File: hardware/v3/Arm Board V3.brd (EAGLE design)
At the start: 165.1 x 76.2 mm, 75 parts, among them CN1 1X4-BIG, IC1 L6208D, IC2 L6208D, IC3 L6208D, IC4 7812TV, IC5 7812TV, IC6 7812TV, IC7 7812DT, IC9 7812DT, Q3 Q_LTC490, U1 MAX3468CPA, U2 XBEE-1B3

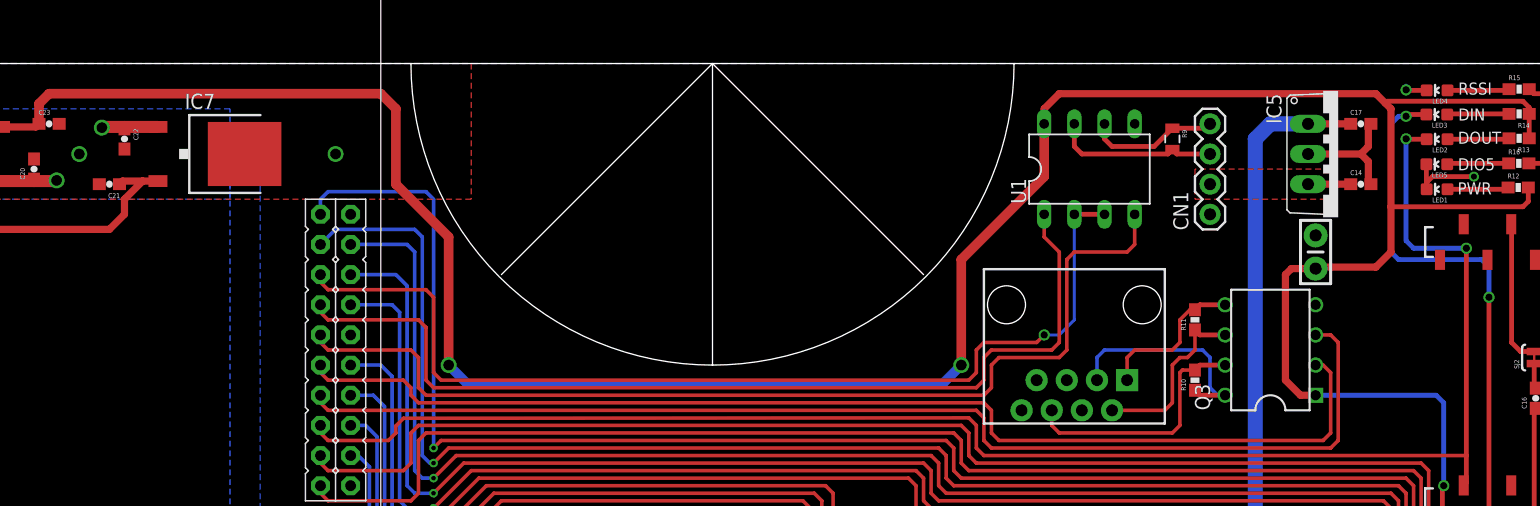
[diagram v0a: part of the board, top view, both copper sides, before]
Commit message: Changed name on l6208 to l6206
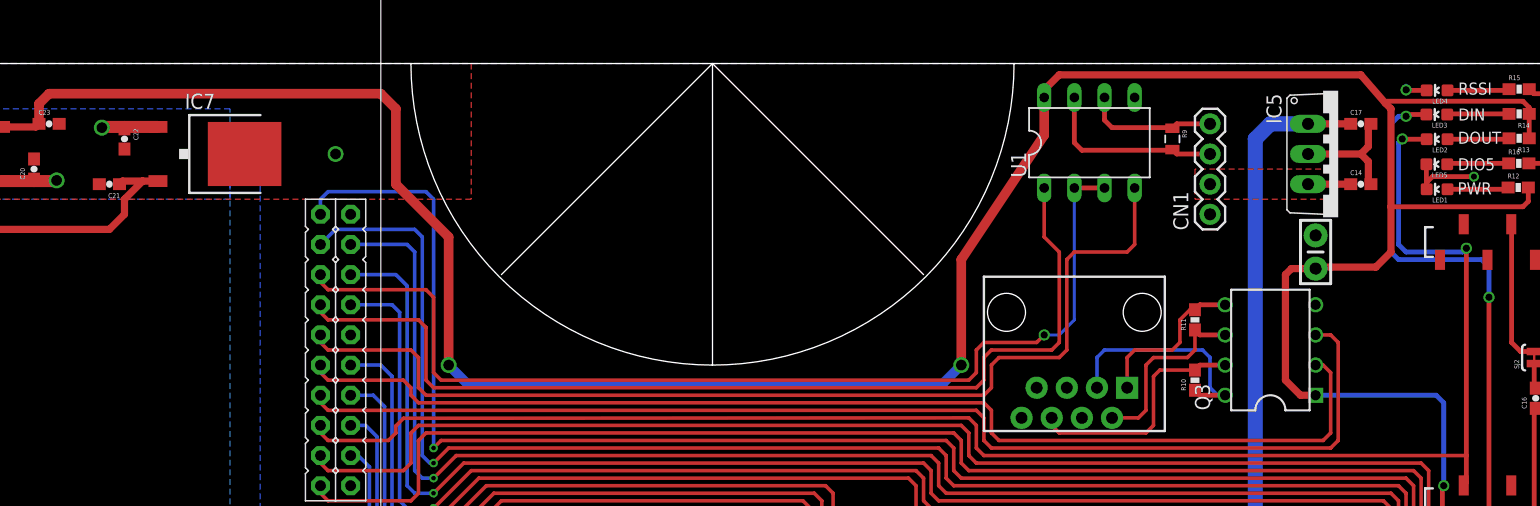
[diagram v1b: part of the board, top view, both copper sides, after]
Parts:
- IC1, IC2, IC3: value L6208D -> L6206D
- moved U1 2.22 mm to (114.3, 69.5)
- moved U$3 0.64 mm to (113.0, 55.2)
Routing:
- net TXD2: track 85.9 -> 88.1 mm
- net RXD2: track 82.1 -> 84.3 mm
- net EN485: track 85.9 -> 88.1 mm
- net DD+: track 13.9 -> 15.7 mm
- net +3V3: track 266.9 -> 268.5 mm
- net RXD3: track 136.7 -> 138.2 mm
- net N$2: track 21.1 -> 20.3 mm
- net N$1: track 15.7 -> 16.3 mm
- net N$5: track 13.1 -> 13.8 mm
- net N$3: track 18.7 -> 19.4 mm
- net GND: vias 9 -> 8

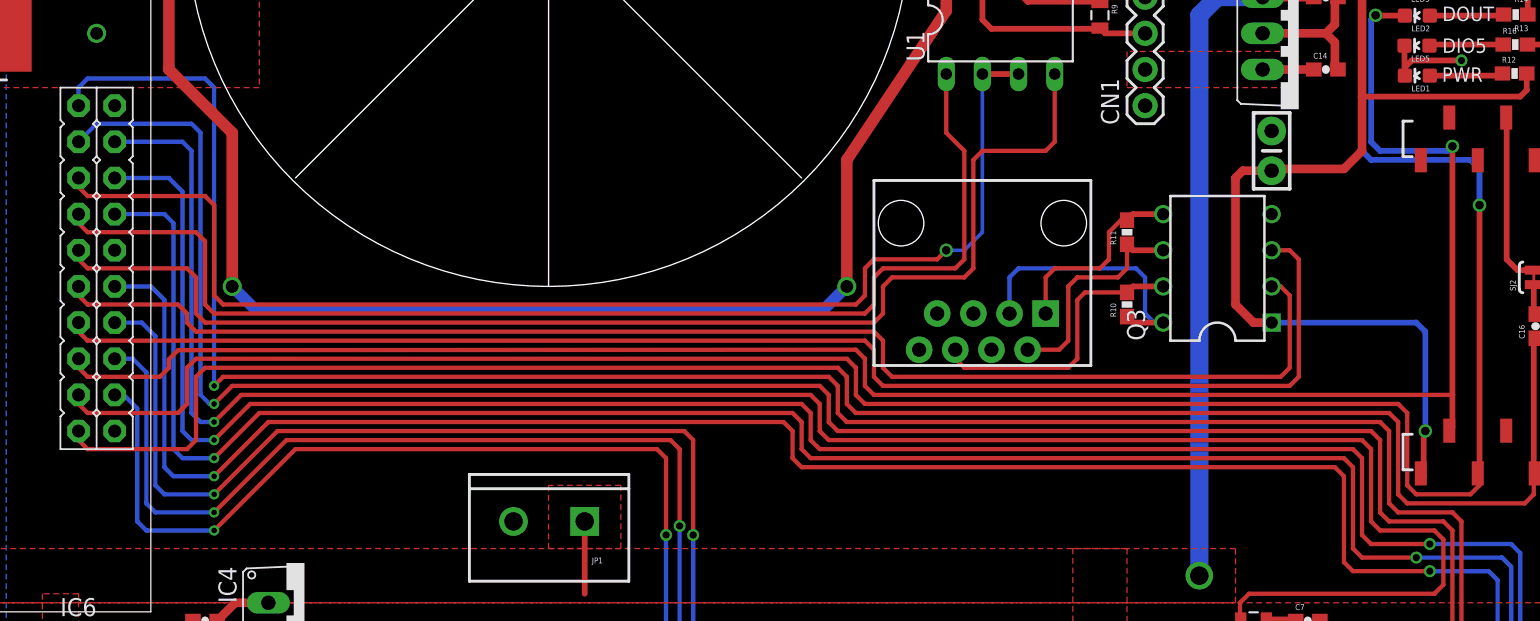
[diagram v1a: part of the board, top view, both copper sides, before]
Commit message: Moved Data Lines closer together
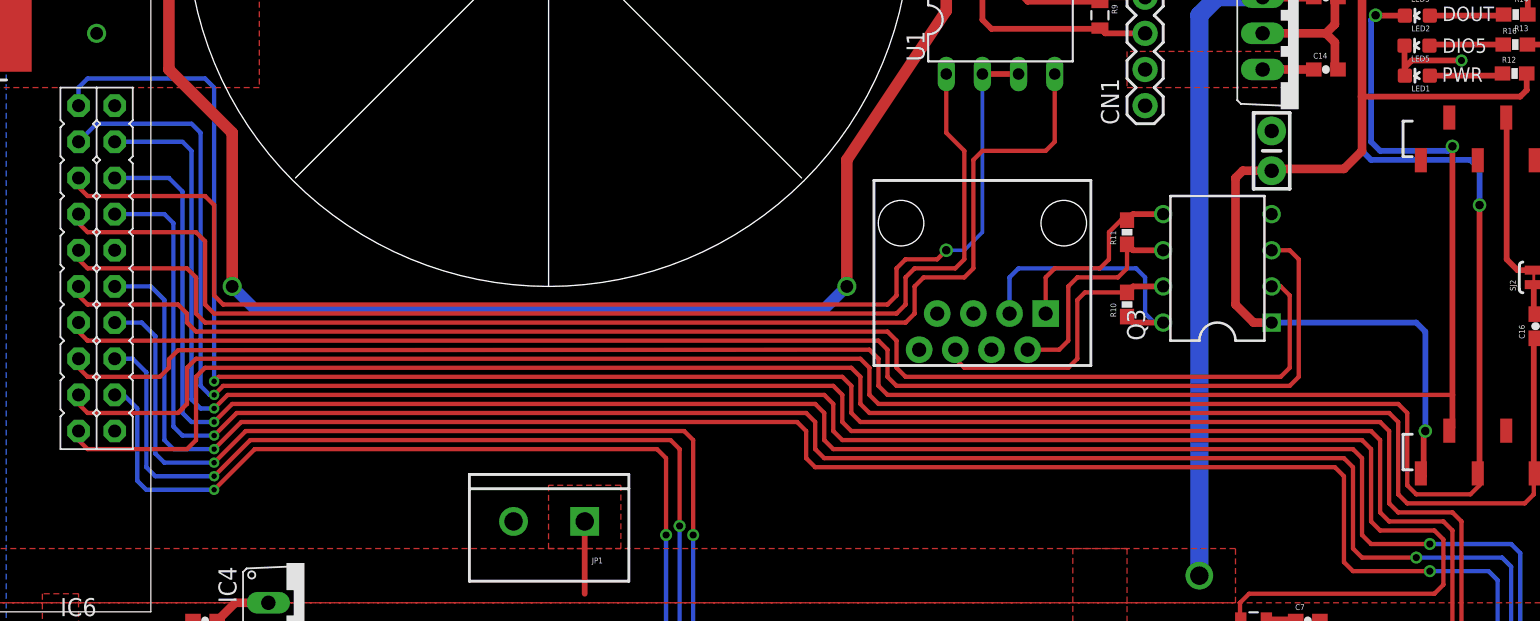
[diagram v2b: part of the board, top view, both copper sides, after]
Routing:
- net IN1_A_3: track 82.5 -> 78.4 mm
- net IN2_A_3: track 85.6 -> 82.0 mm
- net EN_A_3: track 86.3 -> 83.2 mm
- net EN_A_2: track 142.0 -> 139.3 mm
- net IN2_A_2: track 153.1 -> 150.8 mm
- net IN1_A_2: track 156.9 -> 155.1 mm
- net EN_B_2: track 140.7 -> 139.3 mm
- net IN2_B_2: track 135.5 -> 134.6 mm

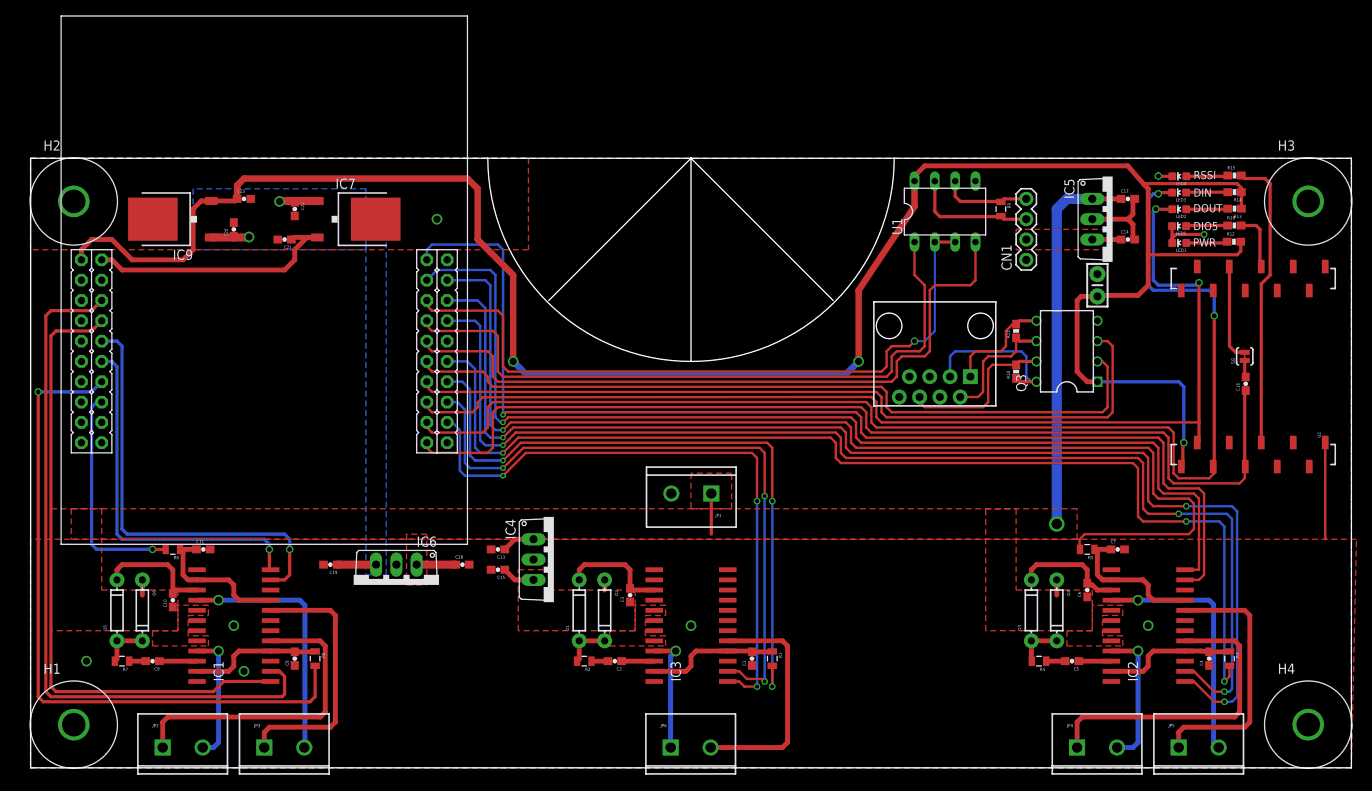
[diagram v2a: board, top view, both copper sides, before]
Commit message: Finished assigning values and fixing errors
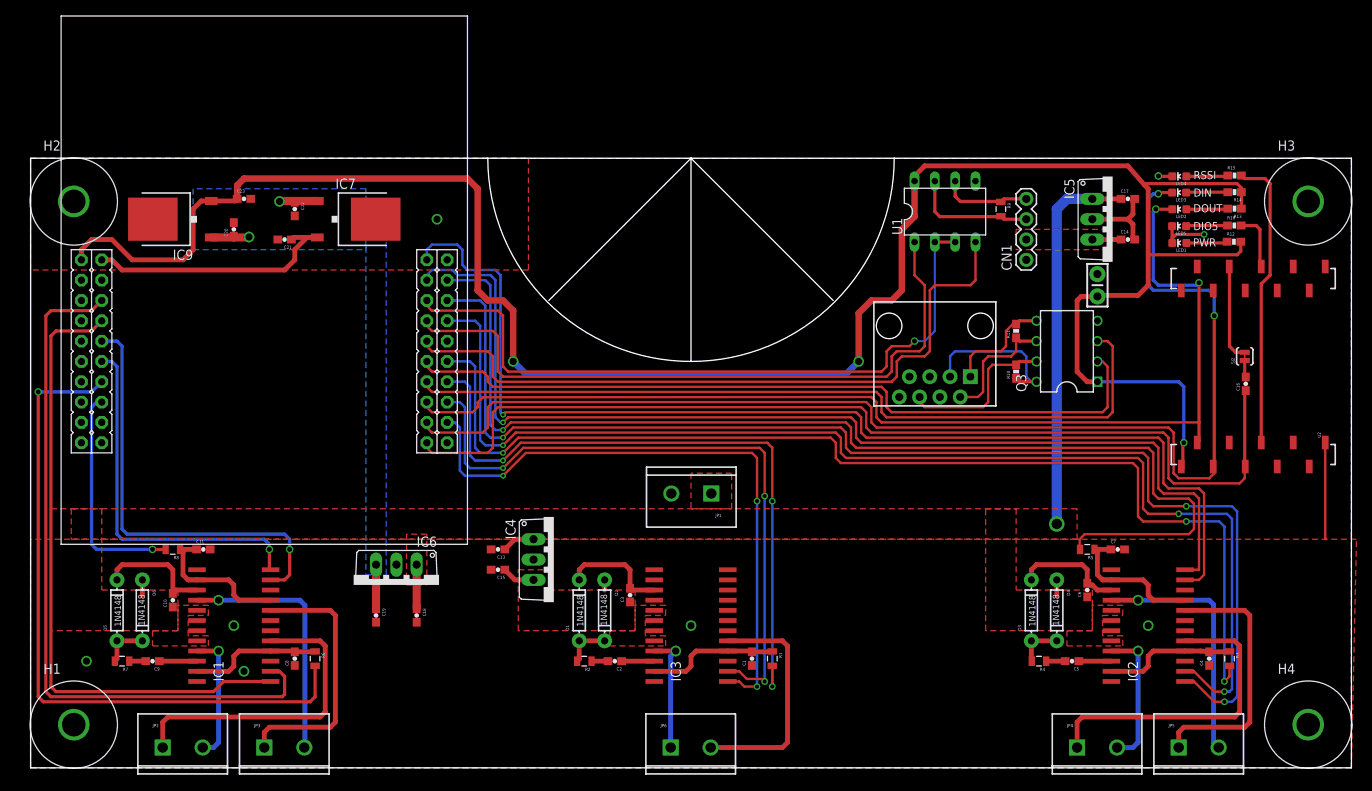
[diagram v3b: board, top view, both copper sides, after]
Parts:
- C1, C11, C4, C7, C8: value 0.1uF -> 5.6nF
- C10, C3, C6: value 0.1uF -> 220nF
- C2, C5, C9: value 0.1uF -> 10nF
- D1, D2, D3, D4, D5, D6: value (none) -> 1N4148
- R1, R3, R5, R6, R8: value (none) -> 100k
- R2, R4, R7: value (none) -> 100
- moved C18 8.54 mm to (48.3, 19.1), turned to 270 degrees
- moved C19 8.54 mm to (43.2, 19.1), turned to 270 degrees
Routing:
- net VIN: track 65.8 -> 61.4 mm
- net +3V3: track 268.5 -> 271.9 mm
- net IN1_B_2: track 140.8 -> 139.9 mm
- net 12V: track 14.7 -> 15.3 mm

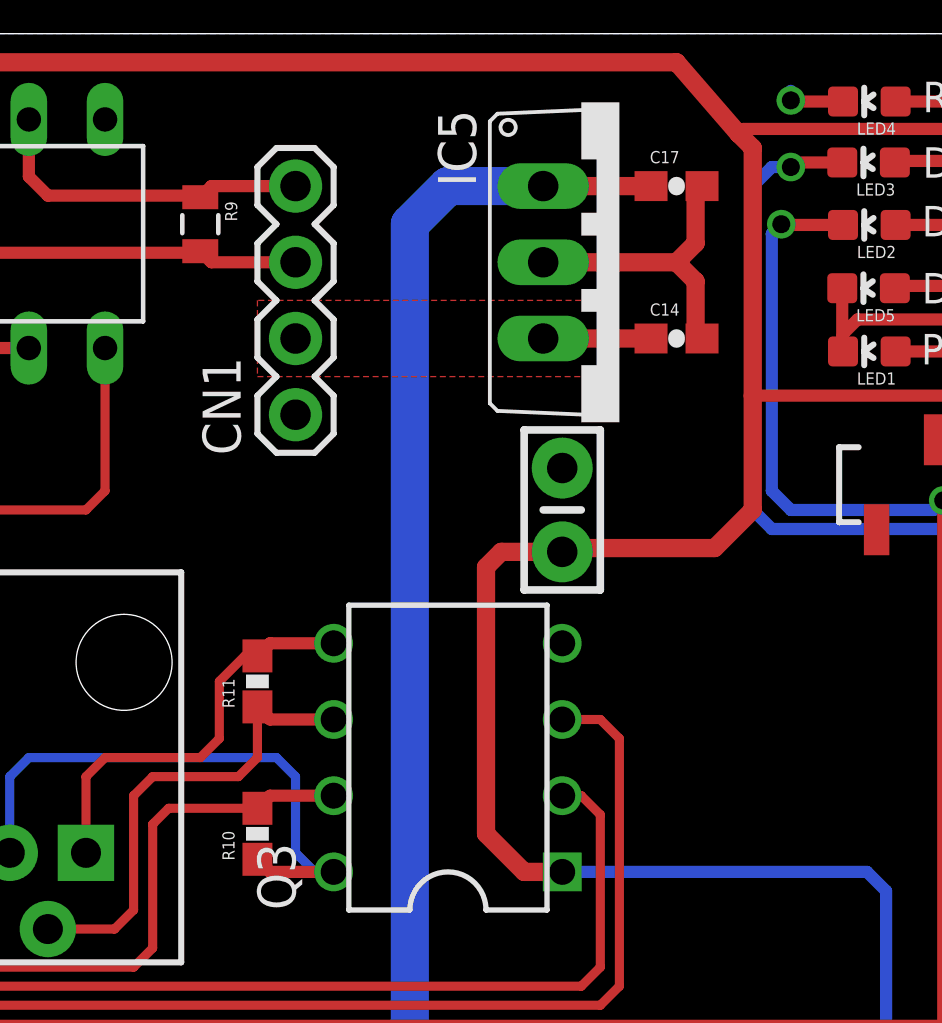
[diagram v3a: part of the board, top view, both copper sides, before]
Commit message: Created and populated BOM
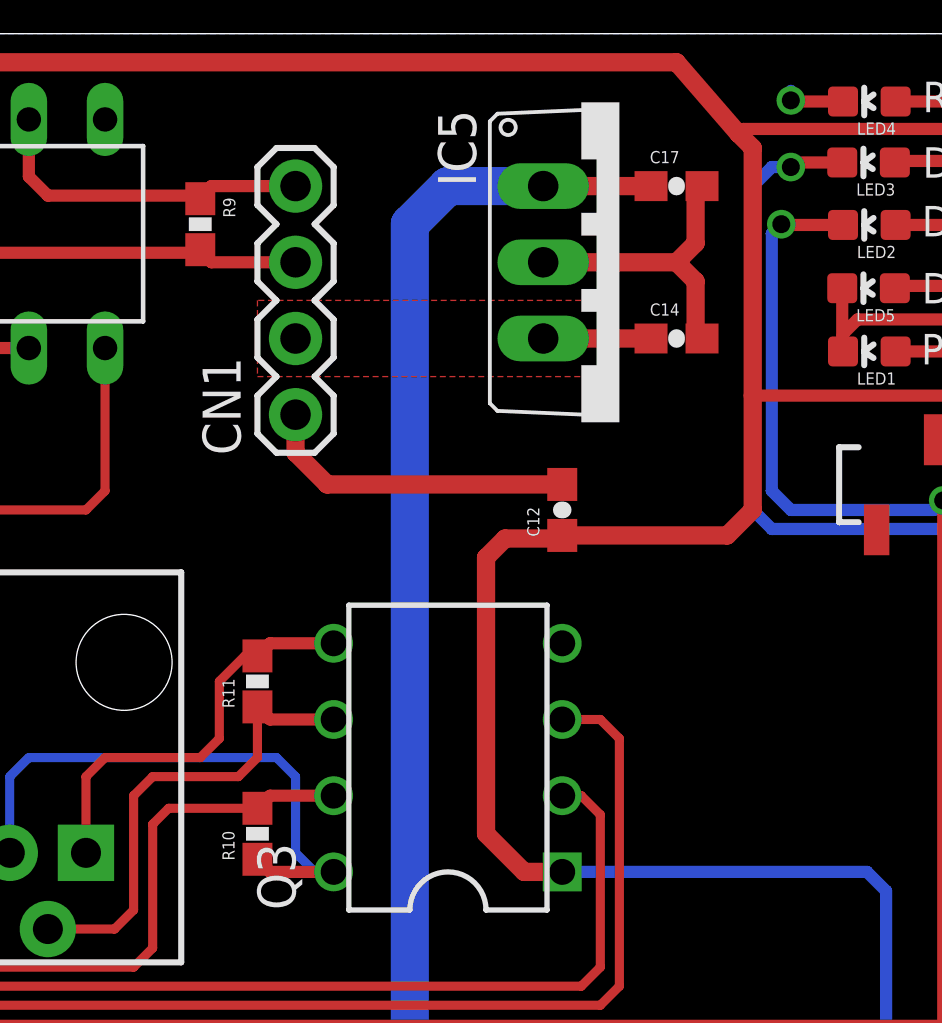
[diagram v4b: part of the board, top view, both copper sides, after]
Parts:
- C12: device SparkFun-Capacitors:CAP-PTH-SMALL-KIT -> SparkFun-Capacitors:0603-CAP
- R9: device SparkFun-Passives:0805 -> SparkFun-Passives:0603-RES
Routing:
- net GND: track 31.3 -> 41.9 mm
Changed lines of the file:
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@@
 <element name="R1" library="SparkFun-Passives" package="0805" value="100k" x="92.71" y="13.6525" rot="R270"/>
 <element name="R2" library="SparkFun-Passives" package="0805" value="100" x="69.215" y="13.335" rot="R180"/>
-<element name="R9" library="SparkFun-Passives" package="0805" value="220" x="121.285" y="69.85" rot="R270"/>
+<element name="R9" library="SparkFun-Passives" package="0603-RES" value="220" x="121.285" y="69.85" rot="R270"/>
 <element name="U1" library="maxim" package="DIL08" value="MAX3468CPA" x="114.3" y="69.5325">
 <attribute name="OC_NEWARK" value="unknown" x="114.3" y="69.5325" size="1.778" layer="27" display="off"/>
@@
 <element name="Q3" library="PCB0M1" package="DIP8" value="Q_LTC490" x="129.54" y="52.07" rot="R90"/>
 <element name="R11" library="SparkFun-Passives" package="0603-RES" value="120 Ohm" x="123.19" y="54.61" rot="R90"/>
-<element name="C12" library="SparkFun-Capacitors" package="CAP-PTH-SMALL-KIT" value=".1uF" x="133.35" y="60.325" rot="R90"/>
+<element name="C12" library="SparkFun-Capacitors" package="0603-CAP" value=".1uF" x="133.35" y="60.325" rot="R90">
+<attribute name="PROD_ID" value="CAP-08604" x="133.35" y="60.325" size="1.778" layer="27" rot="R90" display="off"/>
+<attribute name="VALUE" value="0.1uF" x="133.35" y="60.325" size="1.778" layer="27" rot="R90" display="off"/>
+</element>
 <element name="H1" library="Lib_TH" package="H_MNTHOLE_#4" value="" x="5.3975" y="5.3975"/>
 <element name="H2" library="Lib_TH" package="H_MNTHOLE_#4" value="" x="5.3975" y="70.8025"/>
@@
 <contactref element="IC1" pad="18"/>
 <contactref element="IC1" pad="19"/>
+<wire x1="133.35" y1="61.175" x2="125.515" y2="61.175" width="0.6096" layer="1"/>
+<wire x1="125.515" y1="61.175" x2="124.46" y2="62.23" width="0.6096" layer="1"/>
+<wire x1="124.46" y1="62.23" x2="124.46" y2="63.5" width="0.6096" layer="1"/>
 </signal>
 <signal name="A1_1">
@@
 <wire x1="115.57" y1="71.4375" x2="116.205" y2="70.8025" width="0.4064" layer="1"/>
 <wire x1="116.205" y1="70.8025" x2="121.02" y2="70.8025" width="0.4064" layer="1"/>
-<wire x1="121.02" y1="70.8025" x2="121.285" y2="70.75" width="0.4064" layer="1"/>
+<wire x1="121.02" y1="70.8025" x2="121.285" y2="70.7" width="0.4064" layer="1"/>
 <wire x1="124.46" y1="71.12" x2="121.655" y2="71.12" width="0.4064" layer="1"/>
-<wire x1="121.655" y1="71.12" x2="121.285" y2="70.75" width="0.4064" layer="1"/>
+<wire x1="121.655" y1="71.12" x2="121.285" y2="70.7" width="0.4064" layer="1"/>
 </signal>
 <signal name="DD+" class="1">
@@
 <wire x1="113.03" y1="69.5325" x2="113.665" y2="68.8975" width="0.4064" layer="1"/>
 <wire x1="113.665" y1="68.8975" x2="120.915" y2="68.8975" width="0.4064" layer="1"/>
-<wire x1="120.915" y1="68.8975" x2="121.285" y2="68.95" width="0.4064" layer="1"/>
+<wire x1="120.915" y1="68.8975" x2="121.285" y2="69" width="0.4064" layer="1"/>
 <wire x1="124.46" y1="68.58" x2="121.655" y2="68.58" width="0.4064" layer="1"/>
-<wire x1="121.655" y1="68.58" x2="121.285" y2="68.95" width="0.4064" layer="1"/>
+<wire x1="121.655" y1="68.58" x2="121.285" y2="69" width="0.4064" layer="1"/>
 </signal>
 <signal name="EN485">
@@
 <wire x1="139.7" y1="72.39" x2="139.7" y2="64.135" width="0.6096" layer="1"/>
 <wire x1="139.7" y1="64.135" x2="139.7" y2="60.325" width="0.6096" layer="1"/>
-<wire x1="139.7" y1="60.325" x2="138.43" y2="59.055" width="0.6096" layer="1"/>
-<wire x1="138.43" y1="59.055" x2="133.477" y2="59.055" width="0.6096" layer="1"/>
-<wire x1="133.477" y1="59.055" x2="133.35" y2="58.928" width="0.6096" layer="1"/>
-<wire x1="133.35" y1="58.928" x2="131.318" y2="58.928" width="0.6096" layer="1"/>
-<wire x1="131.318" y1="58.928" x2="130.81" y2="58.42" width="0.6096" layer="1"/>
-<wire x1="130.81" y1="58.42" x2="130.81" y2="49.53" width="0.6096" layer="1"/>
+<wire x1="130.81" y1="58.7375" x2="130.81" y2="49.53" width="0.6096" layer="1"/>
 <wire x1="130.81" y1="49.53" x2="132.08" y2="48.26" width="0.6096" layer="1"/>
 <wire x1="132.08" y1="48.26" x2="133.35" y2="48.26" width="0.6096" layer="1"/>
@@
 <wire x1="105.0925" y1="58.42" x2="103.505" y2="56.8325" width="0.8128" layer="1"/>
 <wire x1="103.505" y1="56.8325" x2="103.505" y2="50.8" width="0.8128" layer="1"/>
+<wire x1="130.81" y1="58.7375" x2="131.445" y2="59.3725" width="0.6096" layer="1"/>
+<wire x1="131.445" y1="59.3725" x2="133.2475" y2="59.3725" width="0.6096" layer="1"/>
+<wire x1="133.2475" y1="59.3725" x2="133.35" y2="59.475" width="0.6096" layer="1"/>
+<wire x1="133.35" y1="59.475" x2="138.85" y2="59.475" width="0.6096" layer="1"/>
+<wire x1="138.85" y1="59.475" x2="139.7" y2="60.325" width="0.6096" layer="1"/>
 </signal>
 <signal name="N$5">
